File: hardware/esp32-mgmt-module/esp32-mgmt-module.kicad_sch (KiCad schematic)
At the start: 91 parts, among them J1 Bus_PCI_Express_x1, J2 BOOT, J3 RJ45_Hanrun_HR913550A_Horizon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, J4 GPIO, J5 SWD, J6 USB_C, J7 UART, Q1 MMBT3904, Q2 MMBT3904, SW1 RESET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

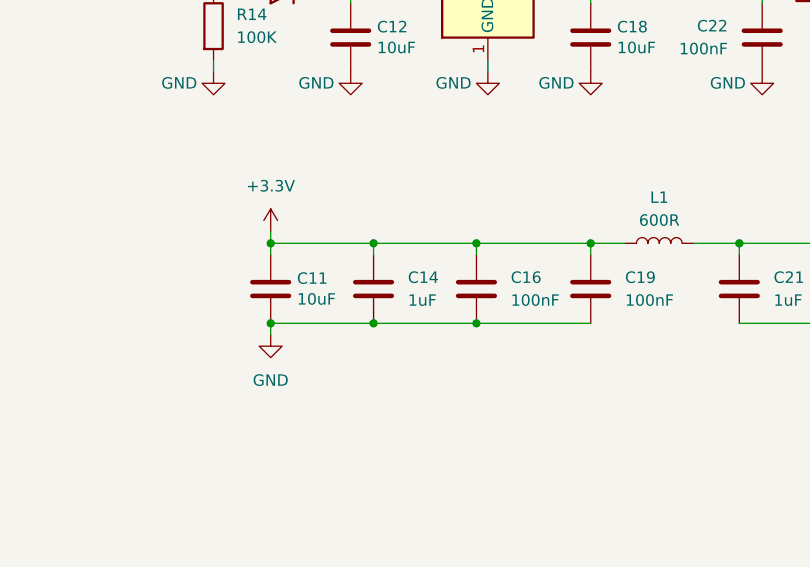
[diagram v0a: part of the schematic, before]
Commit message: fix: add qr code for serial numbers
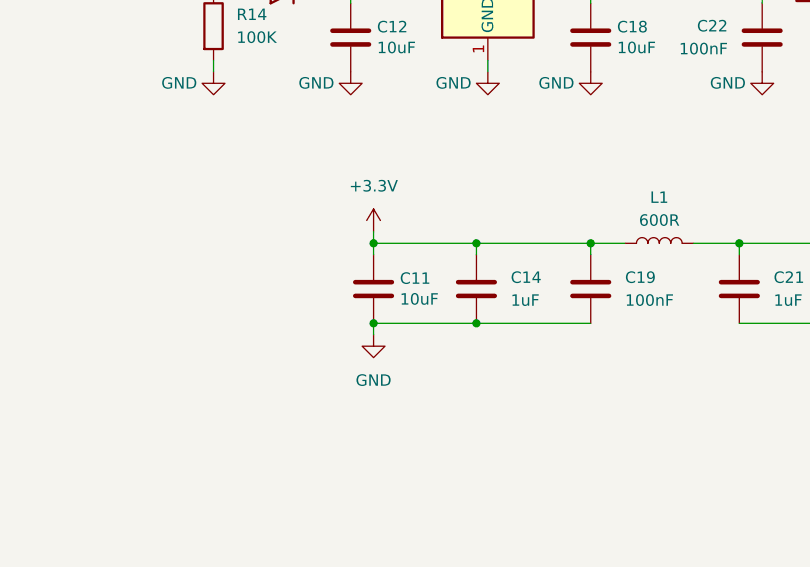
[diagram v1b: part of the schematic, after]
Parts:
- removed C16: 100nF, Capacitor_SMD:C_0402_1005Metric, symbol Device:C
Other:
- moved on the sheet: C11, C14
